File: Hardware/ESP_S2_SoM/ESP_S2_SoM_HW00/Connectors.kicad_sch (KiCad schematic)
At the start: 4 parts, among them J1 54722-0604, J101 USB4510-03-1-A

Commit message: working on schematic
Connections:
- net GND: now also J1.17, J1.35
- net SPICLK: now also J1.23
- net SPICS0: now also J1.25
- net SPICS1: now also J1.33
- net SPID: now also J1.19
- net SPIHD: now also J1.29
- net SPIQ: now also J1.21
- net SPIWP: now also J1.27
- net VDD_SPI: now also J1.31

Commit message: lots of work on routing
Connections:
- net SPID is gone; now on net GND: J1.19
- net D-: now also J1.56; no longer J1.57
- net GND: now also J1.13, J1.37, J1.54; no longer J1.11, J1.17, J1.35, J1.55, J1.56
- net IO33: now also J1.57; no longer J1.54
- net IO34: now also J1.39; no longer J1.37
- net IO35: now also J1.41; no longer J1.39
- net IO36: now also J1.43; no longer J1.41
- net IO37: now also J1.45; no longer J1.43
- net IO38: now also J1.47; no longer J1.45
- net IO39: now also J1.49; no longer J1.47
- net IO40: now also J1.51; no longer J1.49
- net IO41: now also J1.53; no longer J1.51
- net IO42: now also J1.55; no longer J1.53
- net RX0: now also J1.15; no longer J1.13
- net TX0: now also J1.17; no longer J1.15
- net SPICLK renamed SPI1
- net SPICS0 renamed SPI2
- net SPICS1 renamed SPI6
- net SPIHD renamed SPI4
- net SPIQ renamed SPI0
- net SPIWP renamed SPI3
- net VDD_SPI renamed SPI5
- new net BATTERY_TEMP: J1.11
- new net SPI7: J1.35

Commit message: Working on PSoM ESP32S2
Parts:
- removed J1: 54722-0604, Component_lib:547220604, symbol Component_lib:54722-0604
- removed J101: USB4510-03-1-A, Component_lib:USB4510031A, symbol Component_lib:USB4510-03-1-A
- added J1: DF40C-60DP-0.4V(51), Component_lib:DF40C-60DP-0.4V(51), symbol Component_lib:DF40C-60DP-0.4V(51)
- added J2: Bare PCB USB C, Component_lib:usb-c-pcb, symbol Component_lib:Bare PCB USB C
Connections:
- net +3V3: now also J1.4, J1.6
- net BATTERY_TEMP: now also J1.11
- net CC1: now also J2.A5 (CC1)
- net CC2: now also J2.B5 (CC2)
- net D+: now also J1.58, J2.A6 (D+), J2.B6 (D+)
- net D-: now also J1.56, J2.A7 (D-), J2.B7 (D-)
- net GND: now also J1.1, J1.12, J1.13, J1.19, J1.2, J1.37, J1.54, J1.59, J1.60, J2.A1 (GND), J2.A12 (GND), J2.B1 (GND), J2.B12 (GND)
- net IO0: now also J1.14
- net IO1: now also J1.16
- net IO10: now also J1.34
- net IO11: now also J1.36
- net IO12: now also J1.38
- net IO13: now also J1.40
- net IO14: now also J1.42
- net IO15: now also J1.44
- net IO16: now also J1.46
- net IO17: now also J1.48
- net IO18: now also J1.50
- net IO2: now also J1.18
- net IO21: now also J1.52
- net IO3: now also J1.20
- net IO33: now also J1.57
- net IO34: now also J1.39
- net IO35: now also J1.41
- net IO36: now also J1.43
- net IO37: now also J1.45
- net IO38: now also J1.47
- net IO39: now also J1.49
- net IO4: now also J1.22
- net IO40: now also J1.51
- net IO41: now also J1.53
- net IO42: now also J1.55
- net IO5: now also J1.24
- net IO6: now also J1.26
- net IO7: now also J1.28
- net IO8: now also J1.30
- net IO9: now also J1.32
- net RX0: now also J1.15
- net SPI0: now also J1.21
- net SPI1: now also J1.23
- net SPI2: now also J1.25
- net SPI3: now also J1.27
- net SPI4: now also J1.29
- net SPI5: now also J1.31
- net SPI6: now also J1.33
- net SPI7: now also J1.35
- net TX0: now also J1.17
- net VBAT: now also J1.7, J1.9
- net VBUS: now also J1.3, J1.5, J2.A4 (VBUS), J2.A9 (VBUS), J2.B4 (VBUS), J2.B9 (VBUS)
- net VSYS: now also J1.10, J1.8

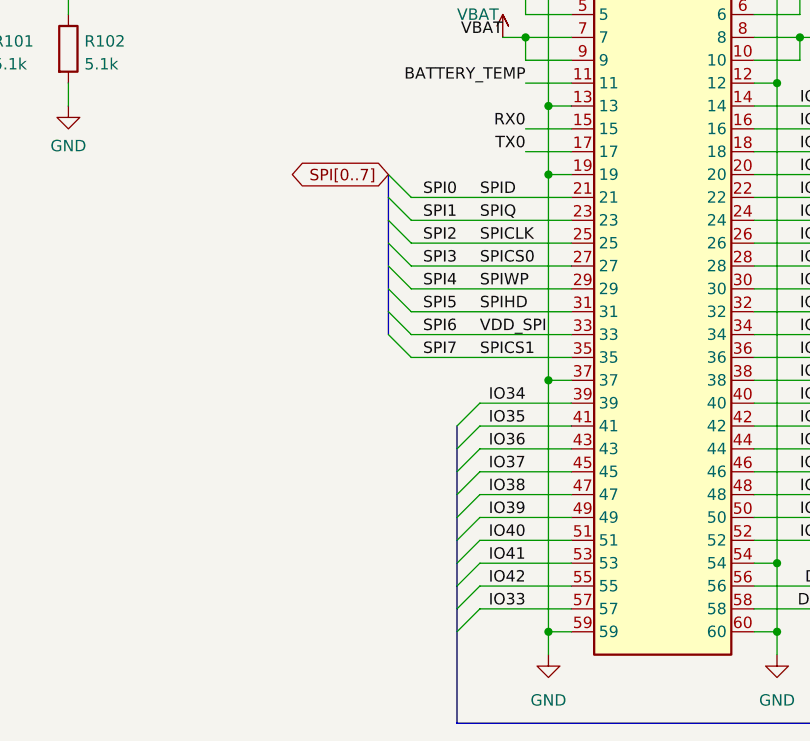
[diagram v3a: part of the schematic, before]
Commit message: Routing ESP32S2
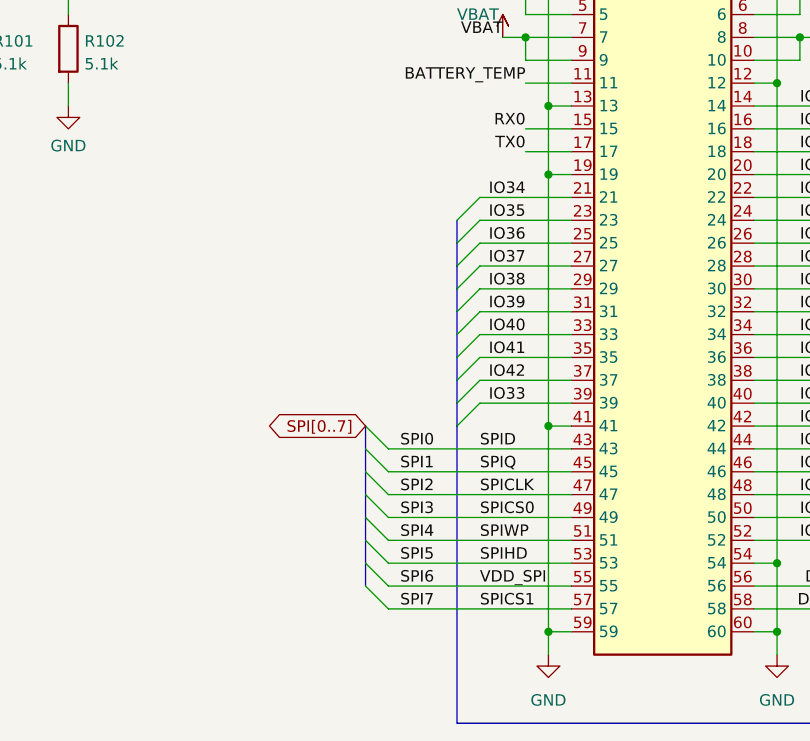
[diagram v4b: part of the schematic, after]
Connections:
- net GND: now also J1.41; no longer J1.37
- net IO33: now also J1.39; no longer J1.57
- net IO34: now also J1.21; no longer J1.39
- net IO35: now also J1.23; no longer J1.41
- net IO36: now also J1.25; no longer J1.43
- net IO37: now also J1.27; no longer J1.45
- net IO38: now also J1.29; no longer J1.47
- net IO39: now also J1.31; no longer J1.49
- net IO40: now also J1.33; no longer J1.51
- net IO41: now also J1.35; no longer J1.53
- net IO42: now also J1.37; no longer J1.55
- net SPI0: now also J1.43; no longer J1.21
- net SPI1: now also J1.45; no longer J1.23
- net SPI2: now also J1.47; no longer J1.25
- net SPI3: now also J1.49; no longer J1.27
- net SPI4: now also J1.51; no longer J1.29
- net SPI5: now also J1.53; no longer J1.31
- net SPI6: now also J1.55; no longer J1.33
- net SPI7: now also J1.57; no longer J1.35

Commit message: Working on routing
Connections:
- net +3V3: no longer J1.4, J1.6
- net BATTERY_TEMP: no longer J1.11
- net GND: now also J1.26; no longer J1.12, J1.13, J1.19
- net IO0: now also J1.28; no longer J1.14
- net IO1: now also J1.3; no longer J1.16
- net IO10: now also J1.21; no longer J1.34
- net IO11: now also J1.23; no longer J1.36
- net IO12: now also J1.25; no longer J1.38
- net IO13: now also J1.27; no longer J1.40
- net IO14: now also J1.29; no longer J1.42
- net IO15: now also J1.31; no longer J1.44
- net IO16: now also J1.33; no longer J1.46
- net IO17: now also J1.35; no longer J1.48
- net IO18: now also J1.37; no longer J1.50
- net IO2: now also J1.5; no longer J1.18
- net IO21: now also J1.39; no longer J1.52
- net IO3: now also J1.7; no longer J1.20
- net IO33: now also J1.30; no longer J1.39
- net IO34: now also J1.32; no longer J1.21
- net IO35: now also J1.34; no longer J1.23
- net IO36: now also J1.36; no longer J1.25
- net IO37: now also J1.38; no longer J1.27
- net IO38: now also J1.40; no longer J1.29
- net IO39: now also J1.42; no longer J1.31
- net IO4: now also J1.9; no longer J1.22
- net IO40: now also J1.44; no longer J1.33
- net IO41: now also J1.46; no longer J1.35
- net IO42: now also J1.48; no longer J1.37
- net IO5: now also J1.11; no longer J1.24
- net IO6: now also J1.13; no longer J1.26
- net IO7: now also J1.15; no longer J1.28
- net IO8: now also J1.17; no longer J1.30
- net IO9: now also J1.19; no longer J1.32
- net RX0: now also J1.52; no longer J1.15
- net SPI0: now also J1.57; no longer J1.43
- net SPI1: now also J1.55; no longer J1.45
- net SPI2: now also J1.53; no longer J1.47
- net SPI3: now also J1.51; no longer J1.49
- net SPI4: now also J1.49; no longer J1.51
- net SPI5: now also J1.47; no longer J1.53
- net SPI6: now also J1.45; no longer J1.55
- net SPI7: now also J1.43; no longer J1.57
- net TX0: now also J1.50; no longer J1.17
- net VBAT: no longer J1.7, J1.9
- net VBUS: no longer J1.3, J1.5
- net VSYS: no longer J1.10, J1.8
